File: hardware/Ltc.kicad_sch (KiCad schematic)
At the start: 20 parts, among them IC1 LTC6804HG-1#PBF

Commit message: spaced out version
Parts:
- removed C? (x4): 10nF, Capacitor_SMD:C_0603_1608Metric, symbol PUTM_EV_BMS_HV_Slave_2021-rescue:C_Small-Device
- removed R49: 100, Resistor_SMD:R_0603_1608Metric, symbol PUTM_EV_BMS_HV_Slave_2021-rescue:R_Small-Device
- removed R? (x4): 10k, Resistor_SMD:R_0603_1608Metric, symbol PUTM_EV_BMS_HV_Slave_2021-rescue:R_Small-Device
- added C?: 100nF, Capacitor_SMD:C_0603_1608Metric, symbol PUTM_EV_BMS_HV_Slave_2021-rescue:C_Small-Device
- added CN1, CN3, CN5, CN7: 100nF, Samacsys:CA064X104K4RACAUTO, symbol ca064x104k4racauto:CA064X104K4RACAUTO
- added R12, R20: 120, Resistor_SMD:R_0603_1608Metric, symbol PUTM_EV_BMS_HV_Slave_2021-rescue:R_Small-Device
- added R2: 10k, Resistor_SMD:R_0603_1608Metric, symbol PUTM_EV_BMS_HV_Slave_2021-rescue:R_Small-Device
- added RN1, RN3, RN5: 100, Samacsys:EXBV8V101JV, symbol exb-v8v101jv:EXB-V8V101JV
- added RN7: 10k, Samacsys:EXBV8V101JV, symbol exb-v8v101jv:EXB-V8V101JV
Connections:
- net DCH1/CO+: now also RN1.3 (R3.1); no longer IC1.24 (C1)
- net DCH10/CO+: now also RN5.2 (R2.1); no longer IC1.2 (C12), IC1.4 (C11)
- net DCH2/CO+: now also RN1.2 (R2.1); no longer IC1.22 (C2)
- net DCH3/CO+: now also RN1.1 (R1.1); no longer IC1.20 (C3)
- net DCH4/CO+: now also RN3.4 (R4.1); no longer IC1.18 (C4)
- net DCH5/CO+: now also RN3.3 (R3.1); no longer IC1.14 (C6), IC1.16 (C5)
- net DCH6/CO+: now also RN3.2 (R2.1); no longer IC1.12 (C7)
- net DCH7/CO+: now also RN3.1 (R1.1); no longer IC1.10 (C8)
- net DCH8/CO+: now also RN5.4 (R4.1); no longer IC1.8 (C9)
- net DCH9/CO+: now also RN5.3 (R3.1); no longer IC1.6 (C10)
- net IMA: now also R12.2
- net IMB: now also R20.2
- net IPA: now also R12.1
- net IPB: now also R20.1
- net TH1+: now also CN7.5 (R4.2), RN7.4 (R4.1)
- net TH2+: now also CN7.6 (R3.2), RN7.3 (R3.1)
- net TH3+: now also CN7.7 (R2.2), RN7.2 (R2.1)
- net TH4+: now also CN7.8 (R1.2), RN7.1 (R1.1)
- net V-: now also C?.2, CN7.1 (R1.1), CN7.2 (R2.1), CN7.3 (R3.1), CN7.4 (R4.1), RN1.4 (R4.1)
- net VREF2: now also R2.2, RN7.5 (R4.2), RN7.6 (R3.2), RN7.7 (R2.2), RN7.8 (R1.2)
- net S6: now reaches IC1.15 (S6)
- net S12: now reaches IC1.3 (S12)
- net TH5+: now reaches IC1.33 (GPIO5)
- net TH5+: now also C?.1, R2.1
- net DCH1/F- renamed C0
- net C0: now also CN1.4 (R4.1), RN1.5 (R4.2)
- net DCH1/S renamed S1
- net DCH10/S renamed S11
- net DCH2/S renamed S2
- net DCH3/S renamed S3
- net DCH4/S renamed S4
- net DCH5/S renamed S5
- net DCH6/S renamed S7
- net DCH7/S renamed S8
- net DCH8/S renamed S9
- net DCH9/S renamed S10
- new net C1: CN1.3 (R3.1), CN1.5 (R4.2), IC1.24 (C1), RN1.6 (R3.2)
- new net C10: CN5.3 (R3.1), CN5.5 (R4.2), IC1.6 (C10), RN5.6 (R3.2)
- new net C11: CN5.2 (R2.1), CN5.6 (R3.2), IC1.2 (C12), IC1.4 (C11), RN5.7 (R2.2)
- new net C2: CN1.2 (R2.1), CN1.6 (R3.2), IC1.22 (C2), RN1.7 (R2.2)
- new net C3: CN1.1 (R1.1), CN1.7 (R2.2), IC1.20 (C3), RN1.8 (R1.2)
- new net C4: CN1.8 (R1.2), CN3.4 (R4.1), IC1.18 (C4), RN3.5 (R4.2)
- new net C5: CN3.3 (R3.1), CN3.5 (R4.2), IC1.14 (C6), IC1.16 (C5), RN3.6 (R3.2)
- new net C7: CN3.2 (R2.1), CN3.6 (R3.2), IC1.12 (C7), RN3.7 (R2.2)
- new net C8: CN3.1 (R1.1), CN3.7 (R2.2), IC1.10 (C8), RN3.8 (R1.2)
- new net C9: CN3.8 (R1.2), CN5.4 (R4.1), IC1.8 (C9), RN5.5 (R4.2)
- no-connect marks 7 -> 10
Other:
- sheet DCH1 ports: added none; removed F+, F-
- sheet DCH10 ports: added none; removed F+, F-
- sheet DCH2 ports: added none; removed F+, F-
- sheet DCH3 ports: added none; removed F+, F-
- sheet DCH4 ports: added none; removed F+, F-
- sheet DCH5 ports: added none; removed F+, F-
- sheet DCH6 ports: added none; removed F+, F-
- sheet DCH7 ports: added none; removed F+, F-
- sheet DCH8 ports: added none; removed F+, F-
- sheet DCH9 ports: added none; removed F+, F-
- moved on the sheet: C18, C19, C?, IC1, Q?, R4, R5, R7, R8

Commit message: finished layout
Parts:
- C18, C19: value 100nf -> 100nF; Manufacturer_Part_Number (none) -> C0603C104K4RAC7867; Mouser Part Number (none) -> 80-C0603C104K4R7867; Mouser Price/Stock (none) -> https://www.mouser.pl/ProductDetail/KEMET/C0603C104K4RAC786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
- C?: Manufacturer_Part_Number (none) -> C0603C104K4RAC7867; Mouser Part Number (none) -> 80-C0603C104K4R7867; Mouser Price/Stock (none) -> https://www.mouser.pl/ProductDetail/KEMET/C0603C104K4RAC786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
- C? (x3): Manufacturer_Part_Number (none) -> CL10B105KB8NQNC; Mouser Part Number (none) -> 187-CL10B105KB8NQNC; Mouser Price/Stock (none) -> https://www.mouser.pl/ProductDetail/Samsung-Electro-Mechani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
- Q?: Manufacturer_Part_Number (none) -> BCP5616QTA; Mouser Part Number (none) -> 621-BCP5616QTA; Mouser Price/Stock (none) -> https://www.mouser.pl/ProductDetail/Diodes-Incorporated/BCP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
- R12, R2, R20, R4, R5, R7, R8: Manufacturer_Part_Number (none) -> --
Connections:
- net TH1+: now also C?.1, R2.1; no longer CN7.5 (R4.2), RN7.4 (R4.1)
- net TH2+: now also CN7.8 (R1.2), RN7.1 (R1.1); no longer CN7.6 (R3.2), RN7.3 (R3.1)
- net TH4+: now also CN7.6 (R3.2), RN7.3 (R3.1); no longer CN7.8 (R1.2), RN7.1 (R1.1)
- net TH5+: now also CN7.5 (R4.2), RN7.4 (R4.1); no longer C?.1, R2.1
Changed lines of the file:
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@@
     (effects (font (size 1.27 1.27)) (justify right))
   )
-  (hierarchical_label "TH2+" (shape input) (at 262.89 45.72 0) (fields_autoplaced)
+  (hierarchical_label "TH2+" (shape input) (at 262.89 40.64 0) (fields_autoplaced)
     (effects (font (size 1.27 1.27)) (justify left))
   )
@@
     (effects (font (size 1.27 1.27)) (justify left))
   )
-  (hierarchical_label "TH5+" (shape input) (at 246.38 40.64 180) (fields_autoplaced)
-    (effects (font (size 1.27 1.27)) (justify right))
+  (hierarchical_label "TH5+" (shape input) (at 262.89 48.26 0) (fields_autoplaced)
+    (effects (font (size 1.27 1.27)) (justify left))
   )
   (hierarchical_label "C6+" (shape input) (at 34.29 95.25 180) (fields_autoplaced)
@@
     (effects (font (size 1.27 1.27)) (justify right))
   )
-  (hierarchical_label "TH1+" (shape input) (at 262.89 48.26 0) (fields_autoplaced)
-    (effects (font (size 1.27 1.27)) (justify left))
+  (hierarchical_label "TH1+" (shape input) (at 246.38 40.64 180) (fields_autoplaced)
+    (effects (font (size 1.27 1.27)) (justify right))
   )
   (hierarchical_label "TH5+" (shape input) (at 193.04 95.25 0) (fields_autoplaced)
@@
     (effects (font (size 1.27 1.27)) (justify left))
   )
-  (hierarchical_label "TH4+" (shape input) (at 262.89 40.64 0) (fields_autoplaced)
+  (hierarchical_label "TH4+" (shape input) (at 262.89 45.72 0) (fields_autoplaced)
     (effects (font (size 1.27 1.27)) (justify left))
   )
@@
     )
     (property "Datasheet" "~" (at 224.79 69.85 0)
+      (effects (font (size 1.27 1.27)) hide)
+    )
+    (property "Manufacturer_Part_Number" "--" (at 224.79 69.85 0)
       (effects (font (size 1.27 1.27)) hide)
     )
@@
       (effects (font (size 1.27 1.27)) hide)
     )
+    (property "Manufacturer_Part_Number" "--" (at 248.92 33.02 0)
+      (effects (font (size 1.27 1.27)) hide)
+    )
     (pin "1")
     (pin "2")
@@
       (effects (font (size 1.27 1.27)) hide)
     )
+    (property "Manufacturer_Name" "" (at 248.92 55.88 0)
+      (effects (font (size 1.27 1.27)) hide)
+    )
+    (property "Manufacturer_Part_Number" "C0603C104K4RAC7867" (at 248.92 55.88 0)
+      (effects (font (size 1.27 1.27)) hide)
+    )
+    (property "Mouser Part Number" "80-C0603C104K4R7867" (at 248.92 55.88 0)
+      (effects (font (size 1.27 1.27)) hide)
+    )
+    (property "Mouser Price/Stock" "https://www.mouser.pl/ProductDetail/KEMET/C0603C104K4RAC7867?qs=l5k%252BbMnNDkktGT%252BFnawJwA%3D%3D" (at 248.92 55.88 0)
+      (effects (font (size 1.27 1.27)) hide)
+    )
     (pin "1")
     (pin "2")
@@
       (effects (font (size 1.27 1.27)) hide)
     )
+    (property "Manufacturer_Part_Number" "--" (at 154.94 49.53 0)
+      (effects (font (size 1.27 1.27)) hide)
+    )
     (pin "1")
     (pin "2")
@@
     )
     (property "Datasheet" "~" (at 200.66 62.23 0)
+      (effects (font (size 1.27 1.27)) hide)
+    )
+    (property "Manufacturer_Part_Number" "--" (at 200.66 62.23 0)
       (effects (font (size 1.27 1.27)) hide)
     )
@@
       (effects (font (size 1.27 1.27)) hide)
     )
+    (property "Manufacturer_Name" "" (at 201.93 125.73 0)
+      (effects (font (size 1.27 1.27)) hide)
+    )
+    (property "Manufacturer_Part_Number" "CL10B105KB8NQNC" (at 201.93 125.73 0)
+      (effects (font (size 1.27 1.27)) hide)
+    )
+    (property "Mouser Part Number" "187-CL10B105KB8NQNC" (at 201.93 125.73 0)
+      (effects (font (size 1.27 1.27)) hide)
+    )
+    (property "Mouser Price/Stock" "https://www.mouser.pl/ProductDetail/Samsung-Electro-Mechanics/CL10B105KB8NQNC?qs=Jm2GQyTW%2FbjBq1uiSyA2AQ%3D%3D" (at 201.93 125.73 0)
+      (effects (font (size 1.27 1.27)) hide)
+    )
     (pin "1")
     (pin "2")
@@
     )
     (property "CBOM" "BCP56-16.115" (at 204.47 77.47 0)
+      (effects (font (size 1.27 1.27)) hide)
+    )
+    (property "Manufacturer_Part_Number" "BCP5616QTA" (at 204.47 77.47 0)
+      (effects (font (size 1.27 1.27)) hide)
+    )
+    (property "Mouser Part Number" "621-BCP5616QTA" (at 204.47 77.47 0)
+      (effects (font (size 1.27 1.27)) hide)
+    )
+    (property "Mouser Price/Stock" "https://www.mouser.pl/ProductDetail/Diodes-Incorporated/BCP5616QTA?qs=%252Bk6%2F5FB6qrmN3CfHeF9FLA%3D%3D" (at 204.47 77.47 0)
       (effects (font (size 1.27 1.27)) hide)
     )
@@
       (effects (font (size 1.27 1.27)) hide)
     )
+    (property "Manufacturer_Part_Number" "--" (at 222.25 118.11 0)
+      (effects (font (size 1.27 1.27)) hide)
+    )
     (pin "1")
     (pin "2")
@@
       (effects (font (size 1.27 1.27)) hide)
     )
+    (property "Manufacturer_Name" "" (at 207.01 90.17 0)
+      (effects (font (size 1.27 1.27)) hide)
+    )
+    (property "Manufacturer_Part_Number" "CL10B105KB8NQNC" (at 207.01 90.17 0)
+      (effects (font (size 1.27 1.27)) hide)
+    )
+    (property "Mouser Part Number" "187-CL10B105KB8NQNC" (at 207.01 90.17 0)
+      (effects (font (size 1.27 1.27)) hide)
+    )
+    (property "Mouser Price/Stock" "https://www.mouser.pl/ProductDetail/Samsung-Electro-Mechanics/CL10B105KB8NQNC?qs=Jm2GQyTW%2FbjBq1uiSyA2AQ%3D%3D" (at 207.01 90.17 0)
+      (effects (font (size 1.27 1.27)) hide)
+    )
     (pin "1")
     (pin "2")
@@
       (effects (font (size 1.27 1.27)) hide)
     )
+    (property "Manufacturer_Name" "" (at 193.04 125.73 0)
+      (effects (font (size 1.27 1.27)) hide)
+    )
+    (property "Manufacturer_Part_Number" "CL10B105KB8NQNC" (at 193.04 125.73 0)
+      (effects (font (size 1.27 1.27)) hide)
+    )
+    (property "Mouser Part Number" "187-CL10B105KB8NQNC" (at 193.04 125.73 0)
+      (effects (font (size 1.27 1.27)) hide)
+    )
+    (property "Mouser Price/Stock" "https://www.mouser.pl/ProductDetail/Samsung-Electro-Mechanics/CL10B105KB8NQNC?qs=Jm2GQyTW%2FbjBq1uiSyA2AQ%3D%3D" (at 193.04 125.73 0)
+      (effects (font (size 1.27 1.27)) hide)
+    )
     (pin "1")
     (pin "2")
@@
       (effects (font (size 1.27 1.27)) (justify left))
     )
-    (property "Value" "100nf" (at 161.163 42.1132 0)
+    (property "Value" "100nF" (at 161.163 42.1132 0)
       (effects (font (size 1.27 1.27)) (justify left))
     )
@@
     )
     (property "Datasheet" "~" (at 160.02 44.45 0)
+      (effects (font (size 1.27 1.27)) hide)
+    )
+    (property "Manufacturer_Name" "" (at 160.02 44.45 0)
+      (effects (font (size 1.27 1.27)) hide)
+    )
+    (property "Manufacturer_Part_Number" "C0603C104K4RAC7867" (at 160.02 44.45 0)
+      (effects (font (size 1.27 1.27)) hide)
+    )
+    (property "Mouser Part Number" "80-C0603C104K4R7867" (at 160.02 44.45 0)
+      (effects (font (size 1.27 1.27)) hide)
+    )
+    (property "Mouser Price/Stock" "https://www.mouser.pl/ProductDetail/KEMET/C0603C104K4RAC7867?qs=l5k%252BbMnNDkktGT%252BFnawJwA%3D%3D" (at 160.02 44.45 0)
       (effects (font (size 1.27 1.27)) hide)
     )
@@
       (effects (font (size 1.27 1.27)) (justify left))
     )
-    (property "Value" "100nf" (at 222.0468 78.613 0)
+    (property "Value" "100nF" (at 222.0468 78.613 0)
       (effects (font (size 1.27 1.27)) (justify left))
     )
@@
     )
     (property "Datasheet" "~" (at 219.71 77.47 0)
+      (effects (font (size 1.27 1.27)) hide)
+    )
+    (property "Manufacturer_Name" "" (at 219.71 77.47 0)
+      (effects (font (size 1.27 1.27)) hide)
+    )
+    (property "Manufacturer_Part_Number" "C0603C104K4RAC7867" (at 219.71 77.47 0)
+      (effects (font (size 1.27 1.27)) hide)
+    )
+    (property "Mouser Part Number" "80-C0603C104K4R7867" (at 219.71 77.47 0)
+      (effects (font (size 1.27 1.27)) hide)
+    )
+    (property "Mouser Price/Stock" "https://www.mouser.pl/ProductDetail/KEMET/C0603C104K4RAC7867?qs=l5k%252BbMnNDkktGT%252BFnawJwA%3D%3D" (at 219.71 77.47 0)
       (effects (font (size 1.27 1.27)) hide)
     )
@@
       (effects (font (size 1.27 1.27)) hide)
     )
+    (property "Manufacturer_Part_Number" "--" (at 200.66 52.07 0)
+      (effects (font (size 1.27 1.27)) hide)
+    )
     (pin "1")
     (pin "2")
@@
       (effects (font (size 1.27 1.27)) hide)
     )
+    (property "Manufacturer_Part_Number" "--" (at 217.17 110.49 0)
+      (effects (font (size 1.27 1.27)) hide)
+    )

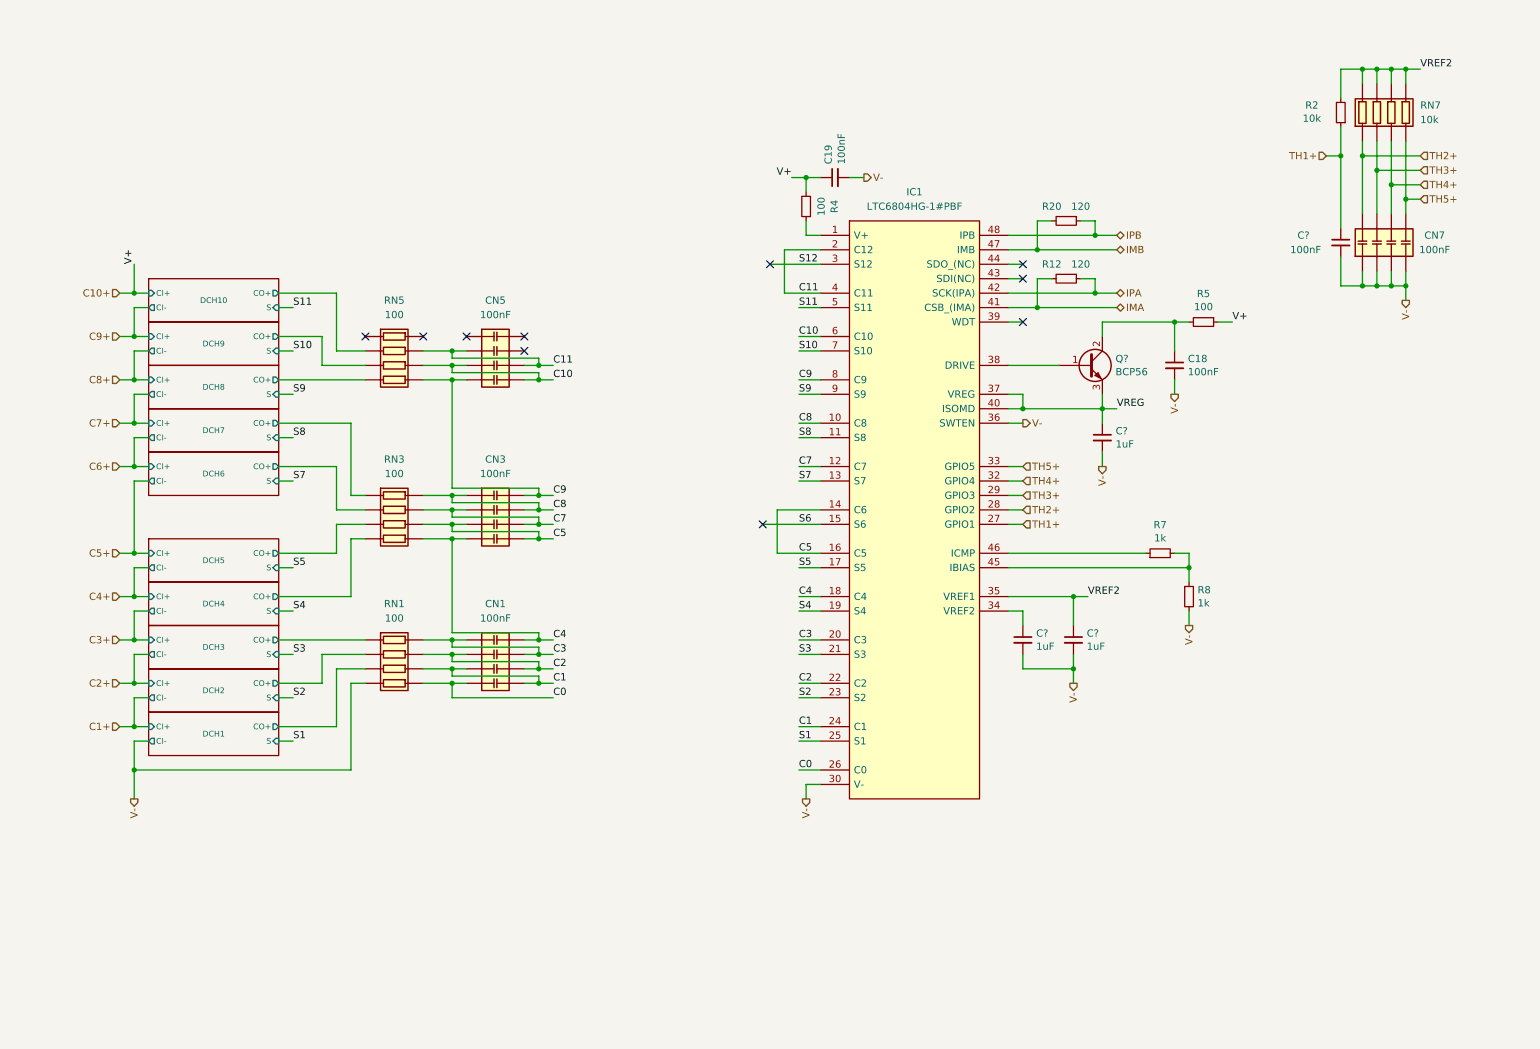
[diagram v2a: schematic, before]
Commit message: change from transformator to capacitive isolation between ltc, change ibias/icmp pin since they are incorrectly connected
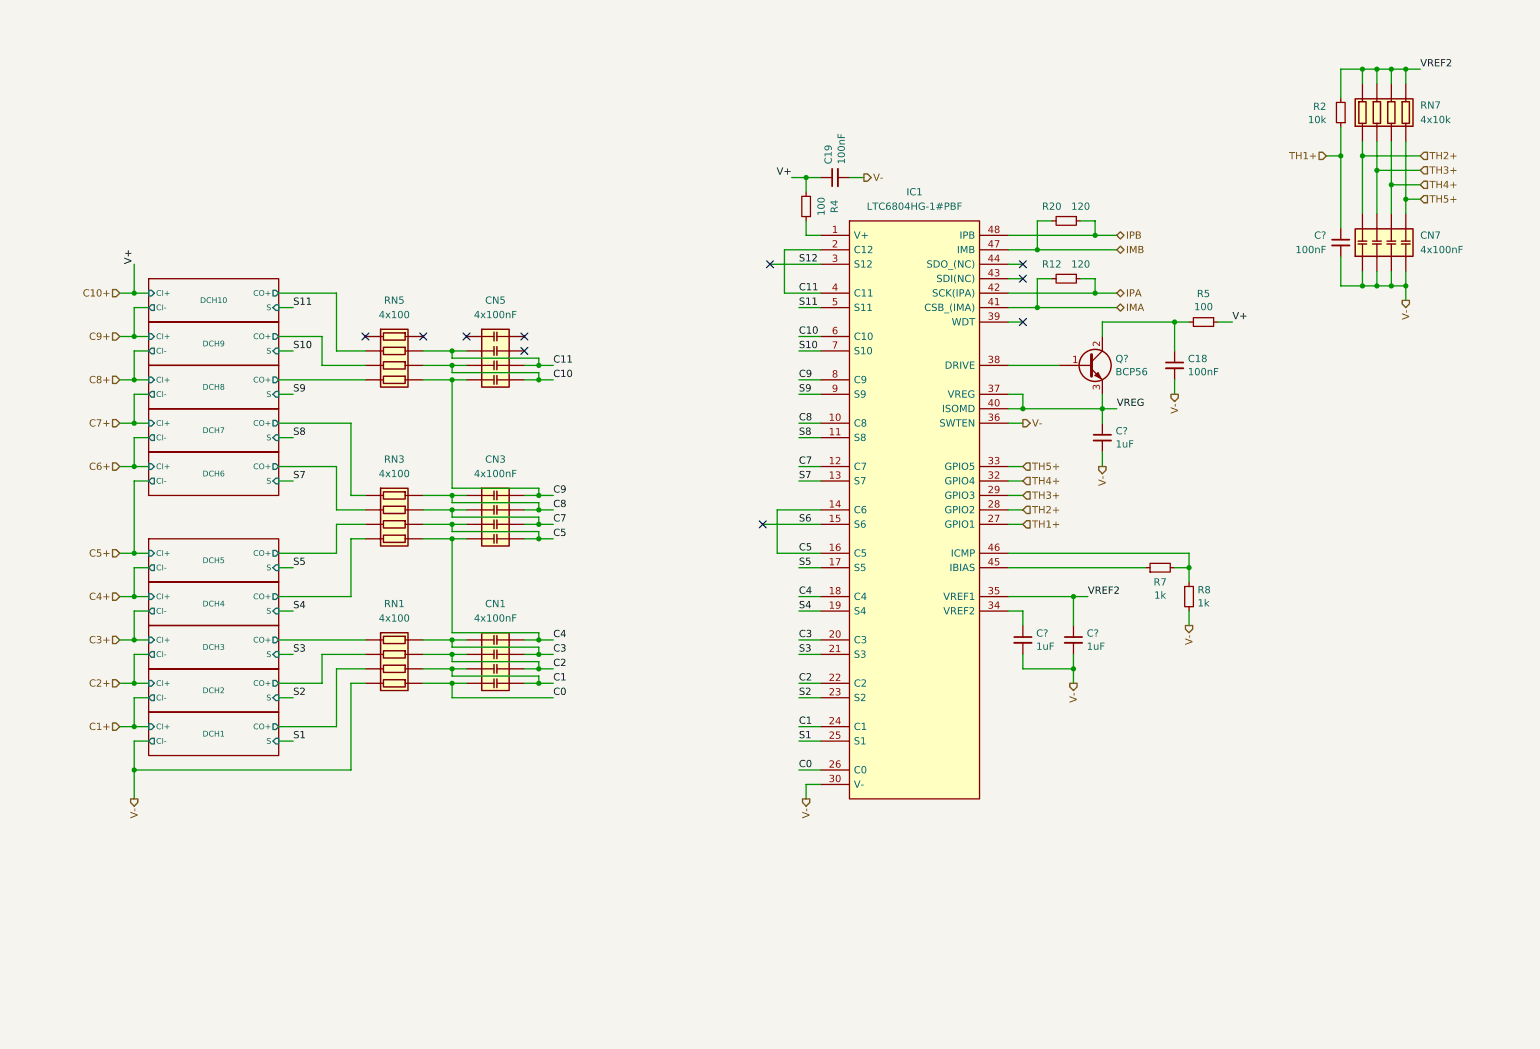
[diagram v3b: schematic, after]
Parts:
- CN1, CN3, CN5, CN7: value 100nF -> 4x100nF
- RN1, RN3, RN5: value 100 -> 4x100
- RN7: value 10k -> 4x10k
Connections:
- net at R7.2, R8.1: now also IC1.46 (ICMP); no longer IC1.45 (IBIAS)
- net at R7.1: now also IC1.45 (IBIAS); no longer IC1.46 (ICMP)
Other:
- moved on the sheet: R7
